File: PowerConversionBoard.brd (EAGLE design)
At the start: 72.4 x 71.1 mm, 33 parts, among them U3 AZ1117EH-3.3TRG1

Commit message: Fixed it for real this time\
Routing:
- net +3.3V: track 194.5 -> 229.4 mm
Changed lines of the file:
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@@
 <wire x1="48.487" y1="13.208" x2="44.196" y2="13.208" width="0.762" layer="1"/>
 <wire x1="41.656" y1="8.636" x2="42.418" y2="9.398" width="0.762" layer="16"/>
-<wire x1="42.418" y1="9.398" x2="42.418" y2="11.43" width="0.762" layer="16"/>
+<wire x1="42.418" y1="9.398" x2="42.418" y2="9.652" width="0.762" layer="16"/>
 <via x="42.418" y="11.43" extent="1-16" drill="0.35"/>
+<wire x1="42.418" y1="9.652" x2="42.418" y2="11.43" width="0.762" layer="16"/>
 <wire x1="42.418" y1="11.43" x2="44.196" y2="13.208" width="0.762" layer="1"/>
 <wire x1="27.94" y1="8.636" x2="41.656" y2="8.636" width="0.762" layer="16"/>
@@
 <via x="58.166" y="9.652" extent="1-16" drill="0.35"/>
 <via x="62.484" y="5.334" extent="1-16" drill="0.35"/>
-<wire x1="58.166" y1="9.652" x2="62.484" y2="5.334" width="0.762" layer="16"/>
+<wire x1="58.166" y1="9.652" x2="60.96" y2="6.858" width="0.762" layer="16"/>
+<wire x1="60.96" y1="6.858" x2="62.484" y2="5.334" width="0.762" layer="16"/>
 <wire x1="62.484" y1="5.334" x2="63.4858125" y2="4.3321875" width="0.762" layer="1"/>
 <wire x1="63.4858125" y1="4.3321875" x2="66.9186875" y2="4.3321875" width="0.762" layer="1"/>
@@
 <wire x1="40.044" y1="10.834" x2="38.1" y2="10.834" width="0.762" layer="1"/>
 <wire x1="42.418" y1="13.208" x2="40.044" y2="10.834" width="0.762" layer="1"/>
-<wire x1="48.487" y1="13.208" x2="54.637" y2="13.208" width="0" layer="19" extent="1-1"/>
+<wire x1="59.055" y1="8.763" x2="58.166" y2="9.652" width="0.762" layer="16"/>
+<wire x1="48.6636" y1="22.4756" x2="48.1296" y2="23.0096" width="0.762" layer="16"/>
+<wire x1="48.1296" y1="23.0096" x2="47.3744" y2="23.0096" width="0.762" layer="16"/>
+<wire x1="43.5356" y1="10.7696" x2="42.418" y2="9.652" width="0.762" layer="16"/>
+<wire x1="58.166" y1="9.652" x2="48.6636" y2="19.1544" width="0.762" layer="16"/>
+<wire x1="48.6636" y1="19.1544" x2="48.6636" y2="22.4756" width="0.762" layer="16"/>
+<wire x1="47.3744" y1="23.0096" x2="43.5356" y2="19.1708" width="0.762" layer="16"/>
+<wire x1="43.5356" y1="19.1708" x2="43.5356" y2="10.7696" width="0.762" layer="16"/>
 </signal>
 <signal name="+5V">

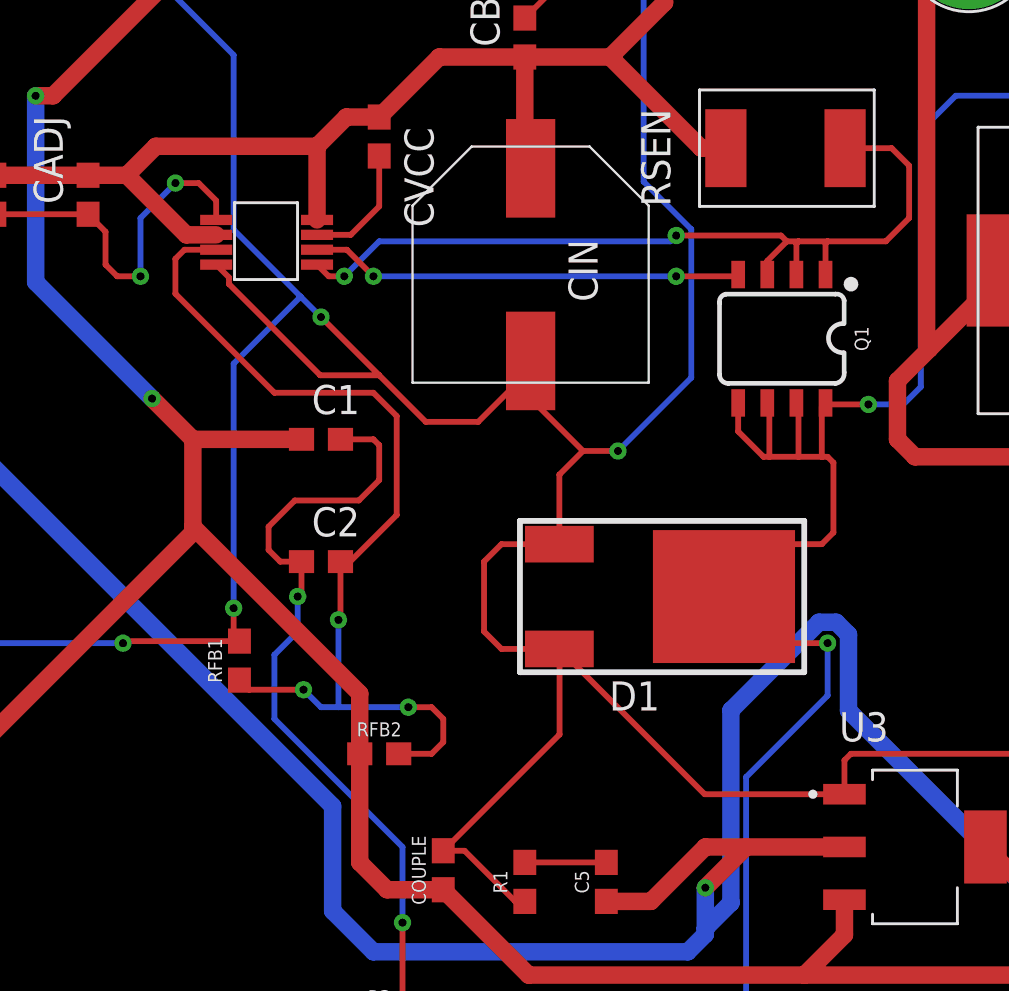
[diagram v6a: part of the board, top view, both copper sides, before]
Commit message: Fixed wire sizing and some of the angles on the board
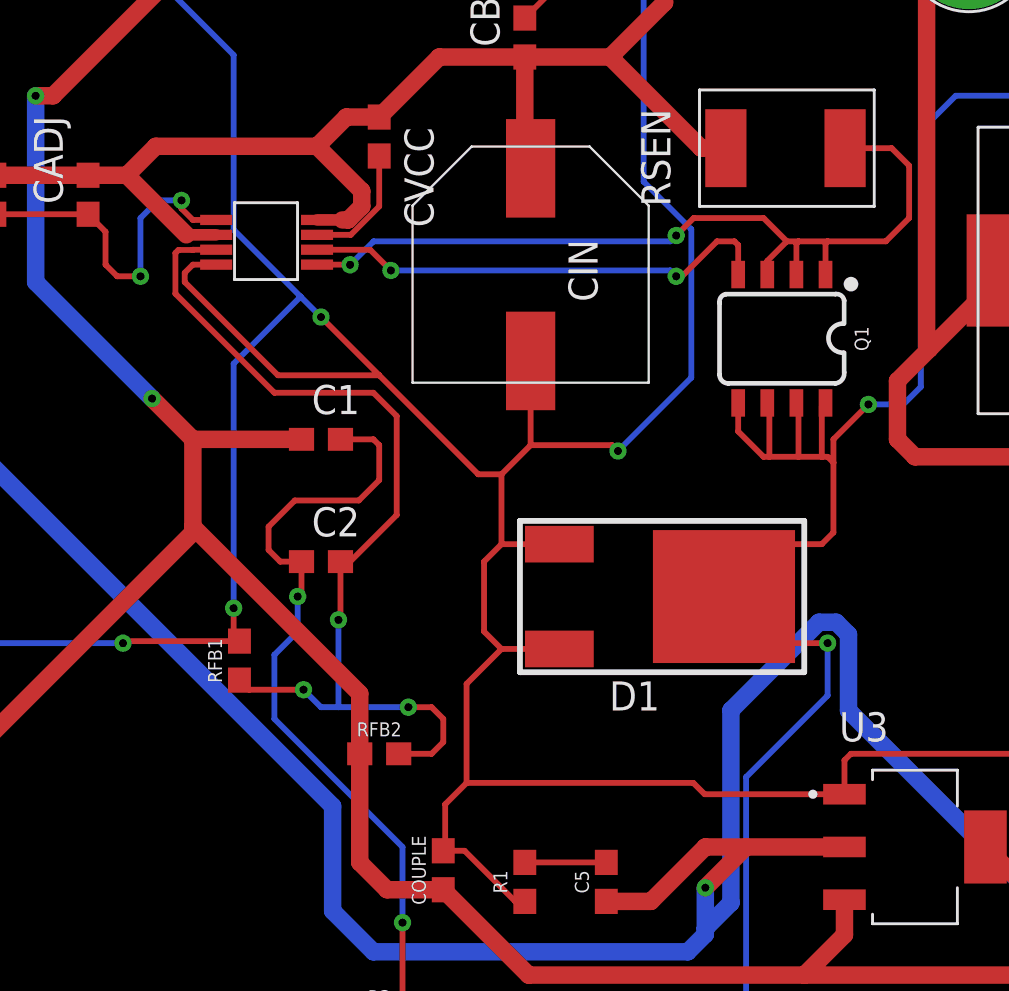
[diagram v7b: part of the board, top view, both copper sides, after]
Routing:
- net GND: track 290.4 -> 294.1 mm
- net +48V: track 135.8 -> 138.4 mm
- net N$7: track 18.9 -> 20.9 mm
- net N$10: track 111.4 -> 112.8 mm
- net N$1: track 15.9 -> 15.0 mm

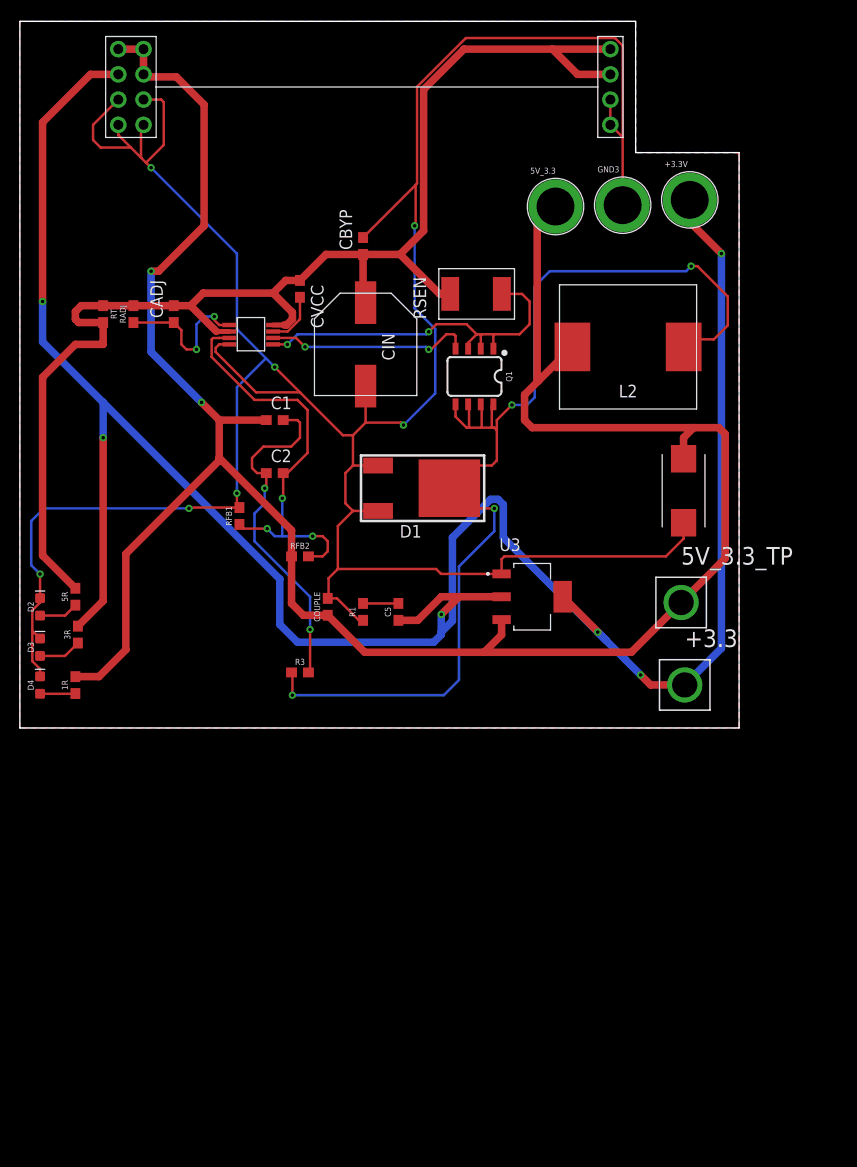
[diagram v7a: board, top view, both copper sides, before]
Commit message: Rough draft of the new and improved board finished; need to work out wires connecting to polygons and probably clean up the test points; there are also a few strange wiring places that need to be cleaned up
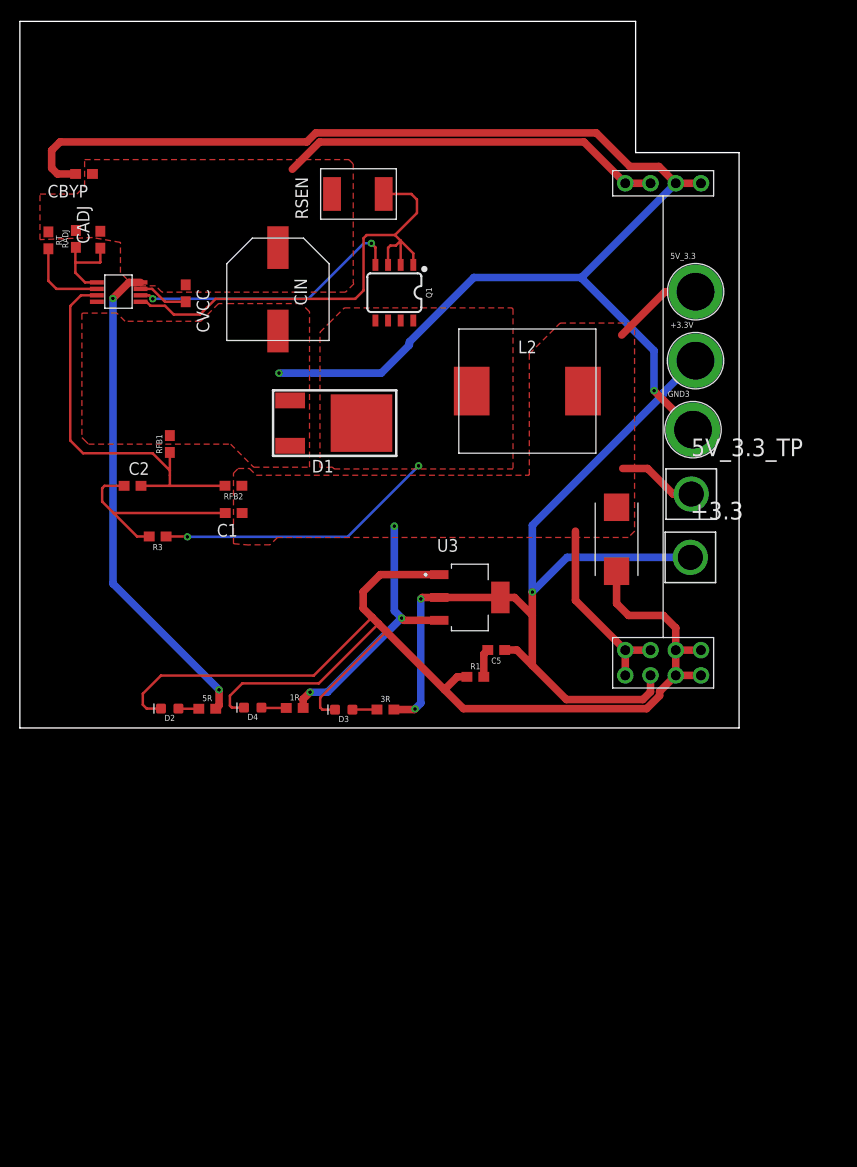
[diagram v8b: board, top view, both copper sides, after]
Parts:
- removed COUPLE: 1nF, SparkFun-Capacitors:0603
- moved U$3 43.0 mm to (64.7, 32.0), turned to 0 degrees
- moved 3R 31.9 mm to (36.8, 1.85), turned to 0 degrees
- moved D3 31.2 mm to (32.6, 1.84), turned to 180 degrees
- moved CBYP 29.0 mm to (6.46, 55.8), turned to 180 degrees
- moved GND3 23.7 mm to (67.8, 30.0)
- moved 1R 22.2 mm to (27.7, 2.01), turned to 0 degrees
- moved D4 21.5 mm to (23.4, 2.05), turned to 180 degrees
- moved R3 19.8 mm to (13.9, 19.3), turned to 180 degrees
- moved 5R 17.4 mm to (18.9, 1.93), turned to 0 degrees
- moved D2 16.6 mm to (15.1, 1.95), turned to 180 degrees
- moved 5V_3.3 16.5 mm to (68.0, 43.9)
- moved +3.3V 16.2 mm to (68.0, 37.0)
- moved RSEN 15.6 mm to (36.6, 53.7)
- moved C2 14.4 mm to (11.3, 24.4)
- moved U$1 14.0 mm to (7.75, 42.9)
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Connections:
- net +5V: no longer COUPLE.1
- net GND: no longer COUPLE.2
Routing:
- net +5V: track 223.5 -> 64.0 mm, vias 2 -> 3
- net +3.3V: track 229.4 -> 99.0 mm, vias 6 -> 3
- net N$10: track 112.8 -> 28.4 mm, vias 4 -> 2
- net +48V: track 138.4 -> 96.7 mm, vias 0 -> 2
- net GND: track 294.1 -> 272.6 mm, vias 7 -> 2
- net N$11: track 34.6 -> 21.1 mm, vias 2 -> 0
- net N$9: track 37.7 -> 50.1 mm, vias 2 -> 0
- net N$7: track 20.9 -> 28.0 mm
- net N$1: track 15.0 -> 9.10 mm, vias 2 -> 0
- net N$13: track 42.2 -> 39.7 mm, vias 3 -> 0
- net N$4: track 3.99 -> 2.06 mm
- net N$5: track 4.35 -> 2.48 mm
- net N$6: track 3.57 -> 2.51 mm
- net N$12: track 3.56 -> 2.87 mm
- added copper zone on layer 1, net +48V
- added copper zone on layer 1, net +5V
- added copper zone on layer 1, net N$10
- removed copper zone on layer 16, net GND
